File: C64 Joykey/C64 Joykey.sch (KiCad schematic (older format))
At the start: 26 parts, among them J1 Port_1, J2 Port_2, M1 Mounting, M2 Mounting, M3 Mounting, M4 Mounting, SW1 FIRE1, SW2 FIRE2, SW3 FIRE3, SW4 UP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

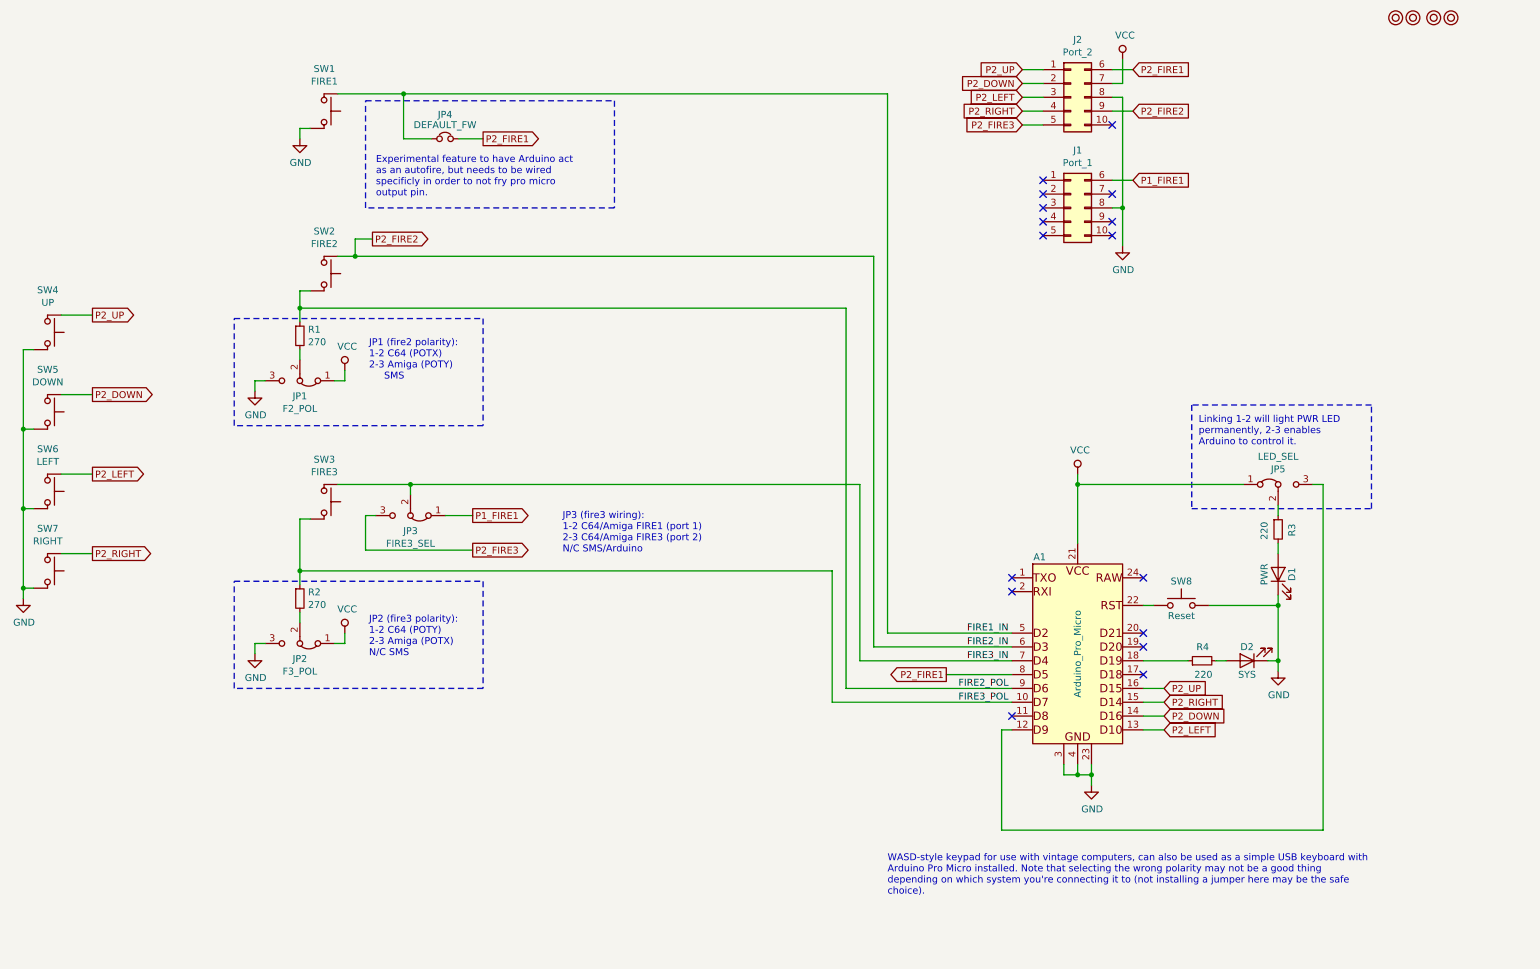
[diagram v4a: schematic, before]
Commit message: Added second DEFAULT_FW so all buttons can be independent
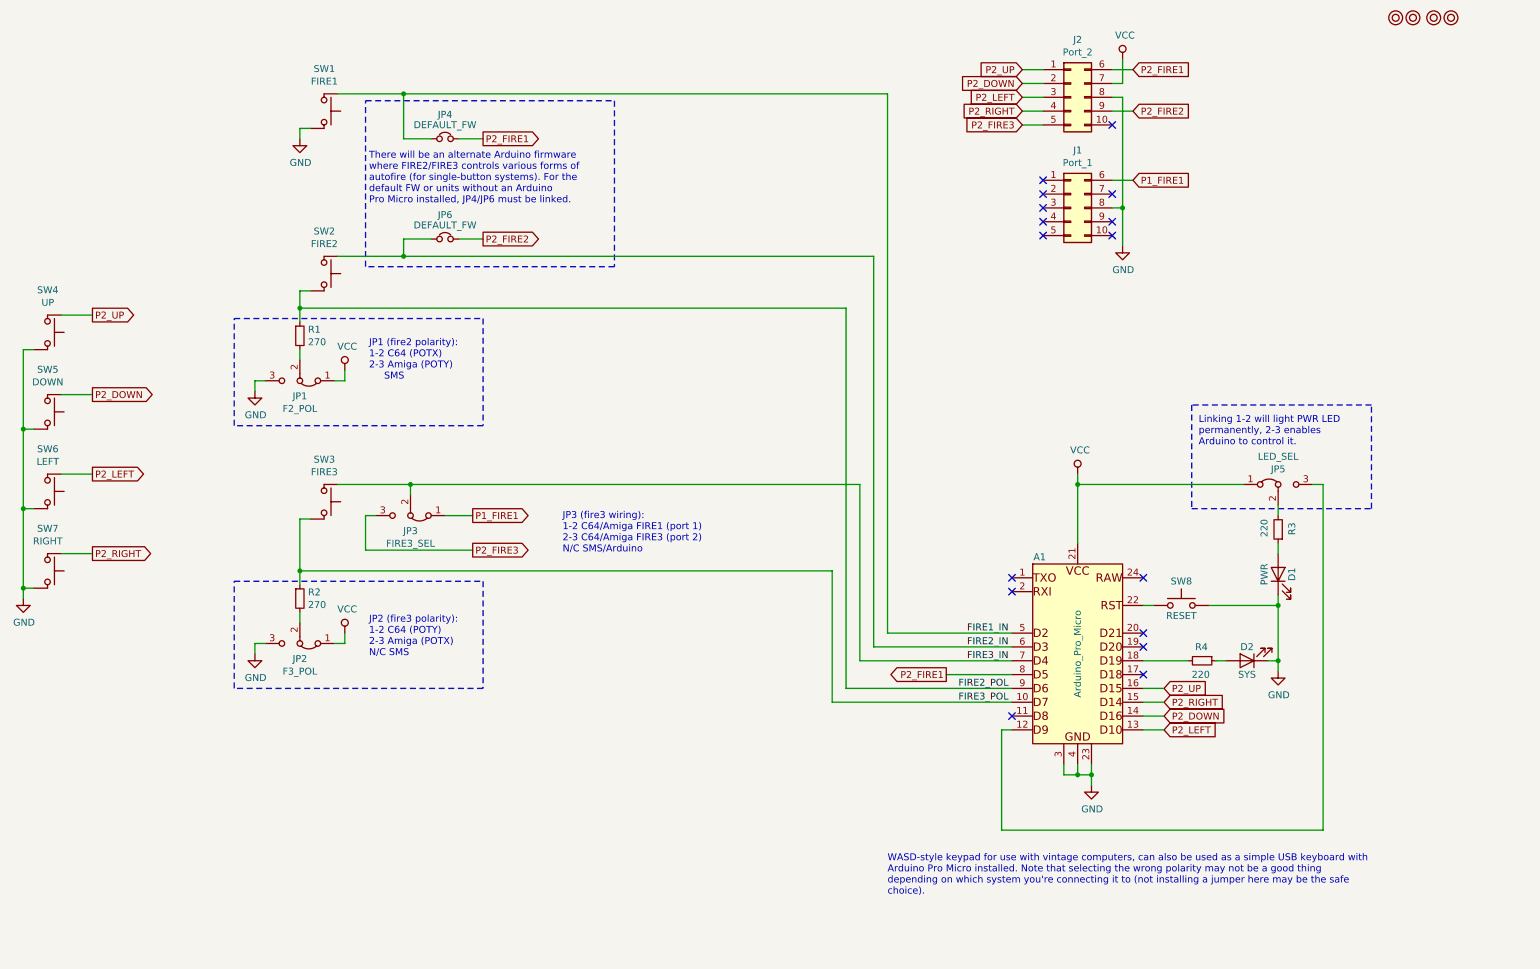
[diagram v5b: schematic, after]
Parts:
- added JP6: DEFAULT_FW, Pin_Headers:Pin_Header_Straight_1x02_Pitch2.54mm, symbol Device:Jumper_NC_Small
- R1, R2, R3, R4: footprint Resistors_THT:R_Axial_DIN0207_L6.3mm_D2.5mm_P7.62mm_Horizontal -> Resistors_THT:R_Axial_DIN0207_L6.3mm_D2.5mm_P10.16mm_Horizontal
- SW8: value Reset -> RESET
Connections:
- net P2_FIRE2: now also JP6.2; no longer A1.6 (D3), SW2.1
- net at A1.18 (D19): now also R4.2; no longer R4.1
- net at D1.2 (A): now also R3.1; no longer R3.2
- net at JP5.2 (C): now also R3.2; no longer R3.1
- net at D2.2 (A): now also R4.1; no longer R4.2
- new net FIRE2_IN: A1.6 (D3), JP6.1, SW2.1
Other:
- note added: "There will be an alternate Arduino firmware\nwhere FIRE2/FIRE3 controls various forms of\nautofire (for single-button systems). For the\ndefault FW or units without an Arduino\nPro Micro installed, JP4/JP6 must be linked."
- note removed: "Experimental feature to have Arduino act\nas an autofire, but needs to be wired\nspecificly in order to not fry pro micro\noutput pin."
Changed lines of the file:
@@
 P2_RIGHT
 Connection ~ 775  4100
-Text GLabel 3300 2150 2    50   Output ~ 0
+Text GLabel 4100 2150 2    50   Output ~ 0
 P2_FIRE2
 Wire Wire Line
@@
 F 0 "R1" H 2834 2896 50  0000 L CNN
 F 1 "270" H 2834 2805 50  0000 L CNN
-F 2 "Resistors_THT:R_Axial_DIN0207_L6.3mm_D2.5mm_P7.62mm_Horizontal" H 2775 2850 50  0001 C CNN
+F 2 "Resistors_THT:R_Axial_DIN0207_L6.3mm_D2.5mm_P10.16mm_Horizontal" H 2775 2850 50  0001 C CNN
 F 3 "~" H 2775 2850 50  0001 C CNN
 	1    2775 2850
@@
 F 0 "R2" H 2834 4796 50  0000 L CNN
 F 1 "270" H 2834 4705 50  0000 L CNN
-F 2 "Resistors_THT:R_Axial_DIN0207_L6.3mm_D2.5mm_P7.62mm_Horizontal" H 2775 4750 50  0001 C CNN
+F 2 "Resistors_THT:R_Axial_DIN0207_L6.3mm_D2.5mm_P10.16mm_Horizontal" H 2775 4750 50  0001 C CNN
 F 3 "~" H 2775 4750 50  0001 C CNN
 	1    2775 4750
@@
 P 9150 4800
 F 0 "SW8" H 9150 4975 50  0000 C CNN
-F 1 "Reset" H 9150 4725 50  0000 C CNN
+F 1 "RESET" H 9150 4725 50  0000 C CNN
 F 2 "Buttons_Switches_THT:SW_PUSH_6mm" H 9150 5000 50  0001 C CNN
 F 3 "~" H 9150 5000 50  0001 C CNN
@@
 U 1 1 5FBD9406
 P 9850 4250
-F 0 "R3" V 9950 4200 50  0000 L CNN
-F 1 "220" V 9750 4175 50  0000 L CNN
-F 2 "Resistors_THT:R_Axial_DIN0207_L6.3mm_D2.5mm_P7.62mm_Horizontal" H 9850 4250 50  0001 C CNN
+F 0 "R3" V 9750 4200 50  0000 L CNN
+F 1 "220" V 9950 4175 50  0000 L CNN
+F 2 "Resistors_THT:R_Axial_DIN0207_L6.3mm_D2.5mm_P10.16mm_Horizontal" H 9850 4250 50  0001 C CNN
 F 3 "~" H 9850 4250 50  0001 C CNN
 	1    9850 4250
-	1    0    0    -1
+	-1   0    0    1
 $EndComp
 Wire Wire Line
@@
 U 1 1 5FBDF2FF
 P 9300 5200
-F 0 "R4" V 9400 5150 50  0000 L CNN
-F 1 "220" V 9200 5125 50  0000 L CNN
-F 2 "Resistors_THT:R_Axial_DIN0207_L6.3mm_D2.5mm_P7.62mm_Horizontal" H 9300 5200 50  0001 C CNN
+F 0 "R4" V 9200 5150 50  0000 L CNN
+F 1 "220" V 9400 5125 50  0000 L CNN
+F 2 "Resistors_THT:R_Axial_DIN0207_L6.3mm_D2.5mm_P10.16mm_Horizontal" H 9300 5200 50  0001 C CNN
 F 3 "~" H 9300 5200 50  0001 C CNN
 	1    9300 5200
-	0    -1   -1   0
+	0    1    1    0
 $EndComp
 Wire Wire Line
@@
 	6925 2275 6925 5100
 Wire Wire Line
-	3050 2275 3175 2275
-Wire Wire Line
 	6925 5100 7925 5100
 Wire Wire Line
@@
 	7025 5000 7925 5000
 Wire Wire Line
-	3300 2150 3175 2150
-Wire Wire Line
-	3175 2150 3175 2275
-Connection ~ 3175 2275
-Wire Wire Line
-	3175 2275 6925 2275
+	3525 2150 3525 2275
 Connection ~ 3525 1100
 Wire Wire Line
@@
 Wire Notes Line
 	4100 5400 2300 5400
-Text Notes 3325 1850 0    50   ~ 0
-Experimental feature to have Arduino act\nas an autofire, but needs to be wired\nspecificly in order to not fry pro micro\noutput pin.
+Text Notes 3275 1900 0    50   ~ 0
+There will be an alternate Arduino firmware\nwhere FIRE2/FIRE3 controls various forms of\nautofire (for single-button systems). For the\ndefault FW or units without an Arduino\nPro Micro installed, JP4/JP6 must be linked.
 Wire Notes Line
 	3250 1150 5050 1150
 Wire Notes Line
-	3250 1925 3250 1150
-Wire Notes Line
-	5050 1150 5050 1925
-Wire Notes Line
-	5050 1925 3250 1925
+	5050 2350 3250 2350
 Wire Wire Line
 	3525 1100 3525 1425
@@
 Text Notes 7025 6900 0    50   ~ 0
 WASD-style keypad for use with vintage computers, can also be used as a simple USB keyboard with\nArduino Pro Micro installed. Note that selecting the wrong polarity may not be a good thing \ndepending on which system you're connecting it to (not installing a jumper here may be the safe\nchoice).
+Connection ~ 3525 2275
+Wire Wire Line
+	3525 2275 6925 2275
+Wire Wire Line
+	3050 2275 3525 2275
+$Comp
+L Device:Jumper_NC_Small JP6
+U 1 1 5FCB76F7
+P 3825 2150
+F 0 "JP6" H 3825 2325 50  0000 C CNN
+F 1 "DEFAULT_FW" H 3825 2250 50  0000 C CNN
+F 2 "Pin_Headers:Pin_Header_Straight_1x02_Pitch2.54mm" H 3825 2150 50  0001 C CNN
+F 3 "~" H 3825 2150 50  0001 C CNN
+	1    3825 2150
+	1    0    0    -1
+$EndComp
+Wire Wire Line
+	3525 2150 3725 2150
+Wire Wire Line
+	3925 2150 4100 2150
+Wire Notes Line
+	5050 1150 5050 2350
+Wire Notes Line
+	3250 2350 3250 1150
 $EndSCHEMATC

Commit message: Added protection diodes
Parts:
- added D3: 1n4001, Diodes_THT:D_DO-41_SOD81_P10.16mm_Horizontal, symbol Device:D
- added D4: 1n4148, Diodes_THT:D_DO-35_SOD27_P7.62mm_Horizontal, symbol Device:D_Small
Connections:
- net P2_FIRE1: now also D4.2 (A); no longer A1.8 (D5)
- net VCC: now also D3.1 (K); no longer J2.7 (Pin_7)
- new net: D3.2 (A), J2.7 (Pin_7)
- new net FIRE1_OUT: A1.8 (D5), D4.1 (K)
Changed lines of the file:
@@
 NoConn ~ 8650 2125
-Wire Wire Line
-	8650 925  8800 925
 Wire Wire Line
 	8650 1725 8800 1725
@@
 L power:VCC #PWR02
 U 1 1 5FB781A5
-P 8725 850
-F 0 "#PWR02" H 8725 700 50  0001 C CNN
-F 1 "VCC" H 8742 1023 50  0000 C CNN
-F 2 "" H 8725 850 50  0001 C CNN
-F 3 "" H 8725 850 50  0001 C CNN
-	1    8725 850
+P 9650 850
+F 0 "#PWR02" H 9650 700 50  0001 C CNN
+F 1 "VCC" H 9667 1023 50  0000 C CNN
+F 2 "" H 9650 850 50  0001 C CNN
+F 3 "" H 9650 850 50  0001 C CNN
+	1    9650 850
 	1    0    0    -1
 $EndComp
@@
 Wire Wire Line
 	8800 1225 8650 1225
-Text GLabel 4100 1425 2    50   Output ~ 0
-P2_FIRE1
 Text GLabel 8000 1325 0    50   Input ~ 0
 P2_FIRE3
@@
 Wire Wire Line
 	9350 4800 9850 4800
-Text GLabel 7450 5300 0    50   Output ~ 0
+Text GLabel 6275 5300 0    50   Output ~ 0
 P2_FIRE1
 NoConn ~ 8875 5000
@@
 	8725 1125 8725 1925
 Wire Wire Line
-	8650 1025 8725 1025
-Wire Wire Line
-	8725 1025 8725 850
+	9650 1025 9650 850
 Text GLabel 9025 5500 2    50   Input ~ 0
 P2_RIGHT
@@
 Text Label 7900 5200 2    50   ~ 0
 FIRE3_IN
+Wire Wire Line
+	3525 1425 3725 1425
+Text Label 7900 5400 2    50   ~ 0
+FIRE2_POL
+Text Label 7900 5500 2    50   ~ 0
+FIRE3_POL
+Wire Notes Line
+	2300 2725 4100 2725
+Wire Notes Line
+	4100 2725 4100 3500
+Wire Notes Line
+	4100 3500 2300 3500
+Wire Notes Line
+	2300 3500 2300 2725
+Wire Notes Line
+	2300 4625 4100 4625
+Wire Notes Line
+	2300 5400 2300 4625
+Wire Notes Line
+	4100 4625 4100 5400
+Wire Notes Line
+	4100 5400 2300 5400
+Text Notes 3275 1900 0    50   ~ 0
+There will be an alternate Arduino firmware\nwhere FIRE2/FIRE3 controls various forms of\nautofire (for single-button systems). For the\ndefault FW or units without an Arduino\nPro Micro installed, JP4/JP6 must be linked.
+Wire Notes Line
+	3250 1150 5050 1150
+Wire Notes Line
+	5050 2350 3250 2350
+Wire Wire Line
+	3525 1100 3525 1425
+$Comp
+L promicro:Arduino_Pro_Micro A1
+U 1 1 5FBBE539
+P 8400 4850
+F 0 "A1" H 8125 5250 50  0000 C CNN
+F 1 "Arduino_Pro_Micro" V 8400 4550 50  0000 C CNN
+F 2 "arduino_pro_micro:Arduino_Pro_Micro" H 8350 4850 50  0001 C CNN
+F 3 "~" H 8350 4850 50  0001 C CNN
+	1    8400 4850
+	1    0    0    -1
+$EndComp
+$Comp
+L Jumper:Jumper_3_Bridged12 JP5
+U 1 1 60BF4B55
+P 9850 3925
+F 0 "JP5" H 9850 4036 50  0000 C CNN
+F 1 "LED_SEL" H 9850 4127 50  0000 C CNN
+F 2 "solder_bridge:select" H 9850 3925 50  0001 C CNN
+F 3 "~" H 9850 3925 50  0001 C CNN
+	1    9850 3925
+	1    0    0    -1
+$EndComp
+Wire Wire Line
+	9850 4725 9850 4800
+Connection ~ 9850 4800
+Wire Wire Line
+	8400 3925 8400 4350
+Wire Wire Line
+	8400 3925 9600 3925
+Wire Wire Line
+	7925 5700 7850 5700
+Wire Wire Line
+	7850 5700 7850 6425
+Wire Wire Line
+	7850 6425 10175 6425
+Wire Wire Line
+	10175 6425 10175 3925
+Wire Wire Line
+	10175 3925 10100 3925
+Wire Wire Line
+	9850 4075 9850 4150
+NoConn ~ 7925 5600
+Text Notes 9275 3650 0    50   ~ 0
+Linking 1-2 will light PWR LED\npermanently, 2-3 enables\nArduino to control it.
+Wire Notes Line
+	10525 4100 10525 3350
+Wire Notes Line
+	10525 3350 9225 3350
+Wire Notes Line
+	9225 3350 9225 4100
+Wire Notes Line
+	9225 4100 10525 4100
+Text Notes 7025 6900 0    50   ~ 0
+WASD-style keypad for use with vintage computers, can also be used as a simple USB keyboard with\nArduino Pro Micro installed. Note that selecting the wrong polarity may not be a good thing \ndepending on which system you're connecting it to (not installing a jumper here may be the safe\nchoice).
+Connection ~ 3525 2275
+Wire Wire Line
+	3525 2275 6925 2275
+Wire Wire Line
+	3050 2275 3525 2275
+$Comp
+L Device:Jumper_NC_Small JP6
+U 1 1 5FCB76F7
+P 3825 2150
+F 0 "JP6" H 3825 2325 50  0000 C CNN
+F 1 "DEFAULT_FW" H 3825 2250 50  0000 C CNN
+F 2 "Pin_Headers:Pin_Header_Straight_1x02_Pitch2.54mm" H 3825 2150 50  0001 C CNN
+F 3 "~" H 3825 2150 50  0001 C CNN
+	1    3825 2150
+	1    0    0    -1
+$EndComp
+Wire Wire Line
+	3525 2150 3725 2150
+Wire Wire Line
+	3925 2150 4100 2150
+Wire Notes Line
+	5050 1150 5050 2350
+Wire Notes Line
+	3250 2350 3250 1150
+$Comp
+L Device:D D3
+U 1 1 5FCFF93E
+P 9425 1025
+F 0 "D3" H 9425 809 50  0000 C CNN
+F 1 "1n4001" H 9425 900 50  0000 C CNN
+F 2 "Diodes_THT:D_DO-41_SOD81_P10.16mm_Horizontal" H 9425 1025 50  0001 C CNN
+F 3 "~" H 9425 1025 50  0001 C CNN
+	1    9425 1025
+	-1   0    0    1
+$EndComp
+Wire Wire Line
+	8650 925  8800 925
+Wire Wire Line
+	9575 1025 9650 1025
+Wire Wire Line
+	8650 1025 9275 1025
+$Comp
+L power:PWR_FLAG #FLG0101
+U 1 1 5FD15FFC
+P 11025 850
+F 0 "#FLG0101" H 11025 925 50  0001 C CNN
+F 1 "PWR_FLAG" H 11025 1023 50  0000 C CNN
+F 2 "" H 11025 850 50  0001 C CNN
+F 3 "~" H 11025 850 50  0001 C CNN
+	1    11025 850
+	1    0    0    -1
+$EndComp
+$Comp
+L power:VCC #PWR0104
+U 1 1 5FD16D69
+P 10675 850
+F 0 "#PWR0104" H 10675 700 50  0001 C CNN
+F 1 "VCC" H 10692 1023 50  0000 C CNN
+F 2 "" H 10675 850 50  0001 C CNN
+F 3 "" H 10675 850 50  0001 C CNN
+	1    10675 850
+	1    0    0    -1
+$EndComp
+Wire Wire Line
+	10675 850  10675 925
+Wire Wire Line
+	10675 925  11025 925
+Wire Wire Line
+	11025 925  11025 850
+$Comp
+L Device:D_Small D4
+U 1 1 5FD49B7F
+P 6450 5300
+F 0 "D4" H 6450 5095 50  0000 C CNN
+F 1 "1n4148" H 6450 5186 50  0000 C CNN
+F 2 "Diodes_THT:D_DO-35_SOD27_P7.62mm_Horizontal" V 6450 5300 50  0001 C CNN
+F 3 "~" V 6450 5300 50  0001 C CNN
+	1    6450 5300
+	-1   0    0    1
+$EndComp
+Wire Wire Line
+	6275 5300 6350 5300
+Wire Wire Line
+	6550 5300 7925 5300
+Text Label 7900 5300 2    50   ~ 0
+FIRE1_OUT
+Wire Wire Line
+	3925 1425 4100 1425
+Text GLabel 4100 1425 2    50   Output ~ 0
+P2_FIRE1
 $Comp
 L Device:Jumper_NC_Small JP4
@@
 	1    0    0    -1
 $EndComp
-Wire Wire Line
-	3525 1425 3725 1425
-Wire Wire Line
-	3925 1425 4100 1425
-Text Label 7900 5400 2    50   ~ 0
-FIRE2_POL
-Text Label 7900 5500 2    50   ~ 0
-FIRE3_POL
-Wire Wire Line
-	7450 5300 7925 5300
-Wire Notes Line
-	2300 2725 4100 2725
-Wire Notes Line
-	4100 2725 4100 3500
-Wire Notes Line
-	4100 3500 2300 3500
-Wire Notes Line
-	2300 3500 2300 2725
-Wire Notes Line
-	2300 4625 4100 4625
-Wire Notes Line
-	2300 5400 2300 4625
-Wire Notes Line
-	4100 4625 4100 5400
-Wire Notes Line
-	4100 5400 2300 5400
-Text Notes 3275 1900 0    50   ~ 0
-There will be an alternate Arduino firmware\nwhere FIRE2/FIRE3 controls various forms of\nautofire (for single-button systems). For the\ndefault FW or units without an Arduino\nPro Micro installed, JP4/JP6 must be linked.
-Wire Notes Line
-	3250 1150 5050 1150
-Wire Notes Line
-	5050 2350 3250 2350
-Wire Wire Line
-	3525 1100 3525 1425
-$Comp
-L promicro:Arduino_Pro_Micro A1
-U 1 1 5FBBE539
-P 8400 4850
-F 0 "A1" H 8125 5250 50  0000 C CNN
-F 1 "Arduino_Pro_Micro" V 8400 4550 50  0000 C CNN
-F 2 "arduino_pro_micro:Arduino_Pro_Micro" H 8350 4850 50  0001 C CNN
-F 3 "~" H 8350 4850 50  0001 C CNN
-	1    8400 4850
-	1    0    0    -1
-$EndComp
-$Comp
-L Jumper:Jumper_3_Bridged12 JP5
-U 1 1 60BF4B55
-P 9850 3925
-F 0 "JP5" H 9850 4036 50  0000 C CNN
-F 1 "LED_SEL" H 9850 4127 50  0000 C CNN
-F 2 "solder_bridge:select" H 9850 3925 50  0001 C CNN
-F 3 "~" H 9850 3925 50  0001 C CNN
-	1    9850 3925
-	1    0    0    -1
-$EndComp
-Wire Wire Line
-	9850 4725 9850 4800
-Connection ~ 9850 4800
-Wire Wire Line
-	8400 3925 8400 4350
-Wire Wire Line
-	8400 3925 9600 3925
-Wire Wire Line
-	7925 5700 7850 5700
-Wire Wire Line
-	7850 5700 7850 6425
-Wire Wire Line
-	7850 6425 10175 6425
-Wire Wire Line
-	10175 6425 10175 3925
-Wire Wire Line
-	10175 3925 10100 3925
-Wire Wire Line
-	9850 4075 9850 4150
-NoConn ~ 7925 5600
-Text Notes 9275 3650 0    50   ~ 0
-Linking 1-2 will light PWR LED\npermanently, 2-3 enables\nArduino to control it.
-Wire Notes Line
-	10525 4100 10525 3350
-Wire Notes Line
-	10525 3350 9225 3350
-Wire Notes Line
-	9225 3350 9225 4100
-Wire Notes Line
-	9225 4100 10525 4100
-Text Notes 7025 6900 0    50   ~ 0
-WASD-style keypad for use with vintage computers, can also be used as a simple USB keyboard with\nArduino Pro Micro installed. Note that selecting the wrong polarity may not be a good thing \ndepending on which system you're connecting it to (not installing a jumper here may be the safe\nchoice).
-Connection ~ 3525 2275
-Wire Wire Line
-	3525 2275 6925 2275
-Wire Wire Line
-	3050 2275 3525 2275
-$Comp
-L Device:Jumper_NC_Small JP6
-U 1 1 5FCB76F7
-P 3825 2150
-F 0 "JP6" H 3825 2325 50  0000 C CNN
-F 1 "DEFAULT_FW" H 3825 2250 50  0000 C CNN
-F 2 "Pin_Headers:Pin_Header_Straight_1x02_Pitch2.54mm" H 3825 2150 50  0001 C CNN
-F 3 "~" H 3825 2150 50  0001 C CNN
-	1    3825 2150
-	1    0    0    -1
-$EndComp
-Wire Wire Line
-	3525 2150 3725 2150
-Wire Wire Line
-	3925 2150 4100 2150
-Wire Notes Line
-	5050 1150 5050 2350
-Wire Notes Line
-	3250 2350 3250 1150
 $EndSCHEMATC

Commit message: Added series resistor to output pin
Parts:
- added R5: 150, Resistors_THT:R_Axial_DIN0207_L6.3mm_D2.5mm_P7.62mm_Horizontal, symbol Device:R_Small
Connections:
- net P2_FIRE1: now also R5.2; no longer D4.2 (A)
- new net: D4.2 (A), R5.1
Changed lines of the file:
@@
 Wire Wire Line
 	9350 4800 9850 4800
-Text GLabel 6275 5300 0    50   Output ~ 0
+Text GLabel 6000 5300 0    50   Output ~ 0
 P2_FIRE1
 NoConn ~ 8875 5000
@@
 $EndComp
 Wire Wire Line
-	6275 5300 6350 5300
-Wire Wire Line
 	6550 5300 7925 5300
 Text Label 7900 5300 2    50   ~ 0
@@
 	1    0    0    -1
 $EndComp
+$Comp
+L Device:R_Small R5
+U 1 1 5FDC0E14
+P 6175 5300
+F 0 "R5" V 6075 5250 50  0000 L CNN
+F 1 "150" V 6275 5225 50  0000 L CNN
+F 2 "Resistors_THT:R_Axial_DIN0207_L6.3mm_D2.5mm_P7.62mm_Horizontal" H 6175 5300 50  0001 C CNN
+F 3 "~" H 6175 5300 50  0001 C CNN
+	1    6175 5300
+	0    1    1    0
+$EndComp
+Wire Wire Line
+	6275 5300 6350 5300
+Wire Wire Line
+	6000 5300 6075 5300
 $EndSCHEMATC
